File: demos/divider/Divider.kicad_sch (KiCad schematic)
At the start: 3 parts

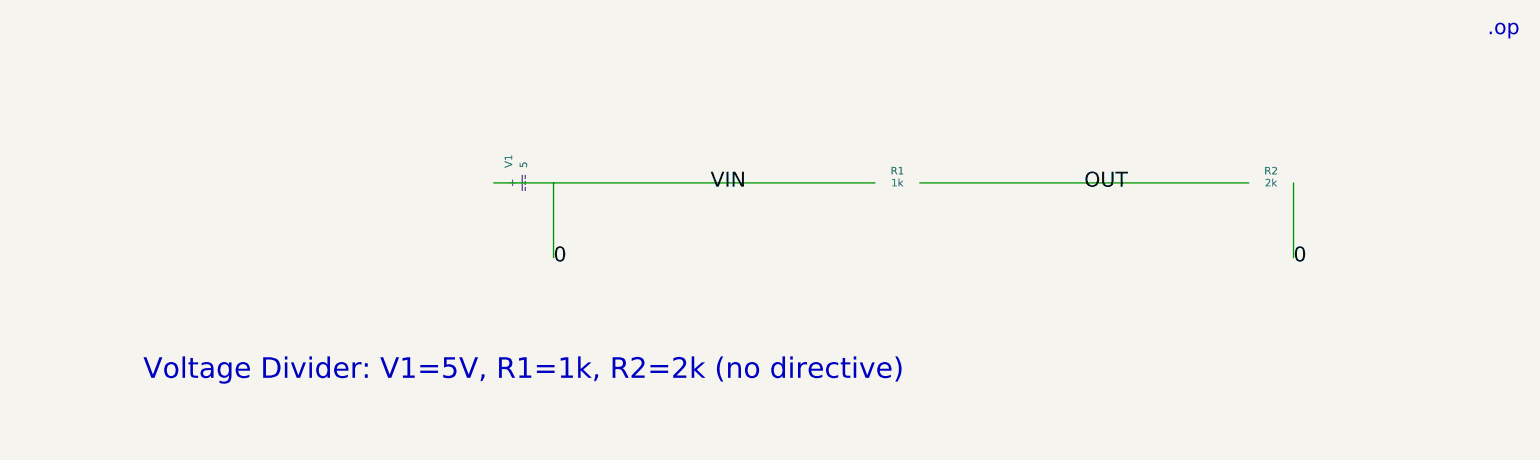
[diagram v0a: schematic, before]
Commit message: feat: Add custom symbol generation for KiCad
- Introduced a new symbol writer module to generate KiCad symbols from specifications.
- Added support for creating custom symbols in a private library, including NE555 and L78L05 components.
- Implemented a command to create symbols from specifications and integrate them into the project's symbol library.
- Developed tests for creating symbols and drawing circuits with custom components, ensuring proper functionality and compliance with ERC.
- Created example scripts for generating symbols from datasheets, specifically for the RP2040 microcontroller.
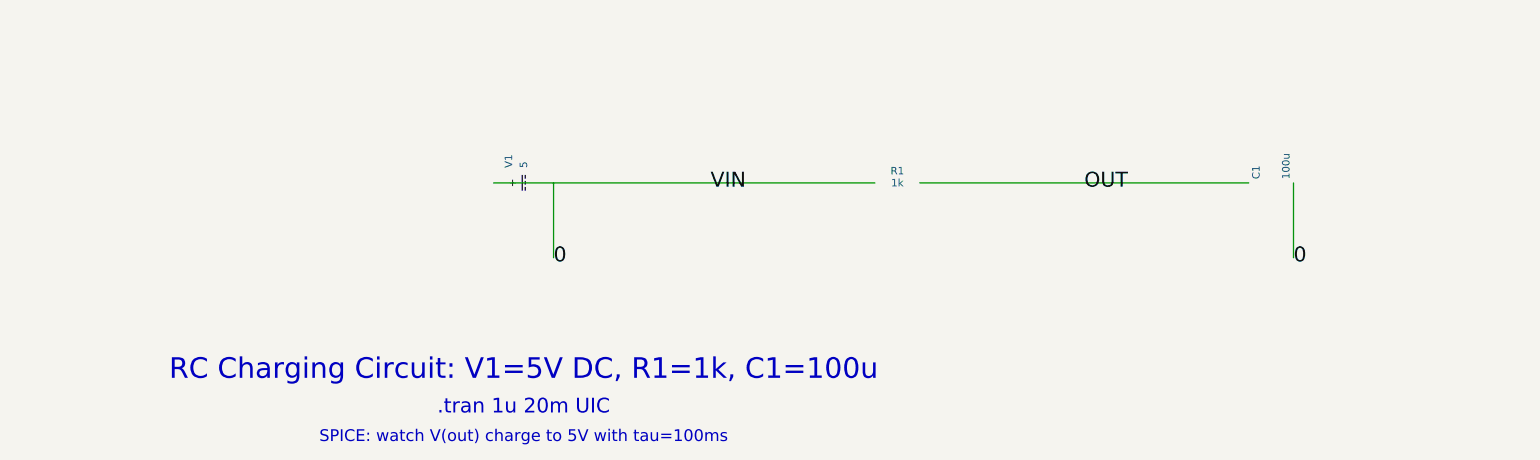
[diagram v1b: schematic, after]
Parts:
- removed R2: 2k, symbol Device:R
- added C1: 100u, symbol Device:C
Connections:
- net 0: now also C1.2
- net OUT: now also C1.1
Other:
- note added: ".tran 1u 20m UIC"
- note added: "RC Charging Circuit: V1=5V DC, R1=1k, C1=100u"
- note added: "SPICE: watch V(out) charge to 5V with tau=100ms"
- note removed: ".op"
- note removed: "Voltage Divider: V1=5V, R1=1k, R2=2k (no directive)"
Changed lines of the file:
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@@
 		(title "Voltage Divider")
 	)
-	(text "Voltage Divider: V1=5V, R1=1k, R2=2k (no directive)"
+	(text ".tran 1u 20m UIC"
+		(exclude_from_sim no)
+		(at 63.5 114.3 0)
+		(effects
+			(font
+				(size 2.5 2.5)
+			)
+		)
+	)
+	(text "RC Charging Circuit: V1=5V DC, R1=1k, C1=100u"
 		(exclude_from_sim no)
 		(at 63.5 107.95 0)
@@
 		)
 	)
-	(text ".op"
-		(exclude_from_sim no)
-		(at 230 50 0)
-		(effects
-			(font
-				(size 2.54 2.54)
-			)
+	(text "SPICE: watch V(out) charge to 5V with tau=100ms"
+		(exclude_from_sim no)
+		(at 63.5 119.38 0)
+		(effects
+			(font
+				(size 2 2)
+			)
+		)
+	)
+	(wire
+		(pts
+			(xy 130.81 76.2) (xy 186.69 76.2)
+		)
+		(stroke
+			(width 0)
+			(type default)
+		)
+	)
+	(wire
+		(pts
+			(xy 58.42 76.2) (xy 123.19 76.2)
+		)
+		(stroke
+			(width 0)
+			(type default)
 		)
 	)
@@
 		)
 	)
-	(wire
-		(pts
-			(xy 130.81 76.2) (xy 186.69 76.2)
-		)
-		(stroke
-			(width 0)
-			(type default)
-		)
-	)
-	(wire
-		(pts
-			(xy 58.42 76.2) (xy 123.19 76.2)
-		)
-		(stroke
-			(width 0)
-			(type default)
+	(label "0"
+		(at 68.58 88.9 0)
+		(effects
+			(font
+				(size 2.54 2.54)
+			)
+		)
+	)
+	(label "OUT"
+		(at 158.75 76.2 0)
+		(effects
+			(font
+				(size 2.54 2.54)
+			)
+		)
+	)
+	(label "0"
+		(at 194.31 88.9 0)
+		(effects
+			(font
+				(size 2.54 2.54)
+			)
 		)
 	)
 	(label "VIN"
 		(at 95.25 76.2 0)
-		(effects
-			(font
-				(size 2.54 2.54)
-			)
-		)
-	)
-	(label "0"
-		(at 68.58 88.9 0)
-		(effects
-			(font
-				(size 2.54 2.54)
-			)
-		)
-	)
-	(label "OUT"
-		(at 158.75 76.2 0)
-		(effects
-			(font
-				(size 2.54 2.54)
-			)
-		)
-	)
-	(label "0"
-		(at 194.31 88.9 0)
 		(effects
 			(font
@@
 			)
 		)
+		(pin "2"
+		)
 		(pin "1"
-		)
-		(pin "2"
 		)
 		(instances
@@
 				(path "/91a1d6ab-baa3-4e2f-aded-405b766975b0"
 					(reference "V1")
+					(unit 1)
+				)
+			)
+		)
+	)
+	(symbol
+		(lib_id "Device:C")
+		(at 190.5 76.2 90)
+		(unit 1)
+		(body_style 0)
+		(exclude_from_sim no)
+		(in_bom yes)
+		(on_board yes)
+		(in_pos_files yes)
+		(dnp no)
+		(property "Reference" "C1"
+			(at 187.96 75.565 0)
+			(show_name no)
+			(do_not_autoplace no)
+			(effects
+				(font
+					(size 1.27 1.27)
+				)
+				(justify left)
+			)
+		)
+		(property "Value" "100u"
+			(at 193.04 75.565 0)
+			(show_name no)
+			(do_not_autoplace no)
+			(effects
+				(font
+					(size 1.27 1.27)
+				)
+				(justify left)
+			)
+		)
+		(property "Footprint" ""
+			(at 194.31 75.2348 0)
+			(hide yes)
+			(show_name no)
+			(do_not_autoplace no)
+			(effects
+				(font
+					(size 1.27 1.27)
+				)
+			)
+		)
+		(property "Datasheet" ""
+			(at 190.5 76.2 0)
+			(hide yes)
+			(show_name no)
+			(do_not_autoplace no)
+			(effects
+				(font
+					(size 1.27 1.27)
+				)
+			)
+		)
+		(property "Description" "Unpolarized capacitor"
+			(at 190.5 76.2 0)
+			(hide yes)
+			(show_name no)
+			(do_not_autoplace no)
+			(effects
+				(font
+					(size 1.27 1.27)
+				)
+			)
+		)
+		(pin "2"
+		)
+		(pin "1"
+		)
+		(instances
+			(project "Divider"
+				(path "/91a1d6ab-baa3-4e2f-aded-405b766975b0"
+					(reference "C1")
 					(unit 1)
 				)
@@
 			)
 		)
+		(pin "1"
+		)
 		(pin "2"
-		)
-		(pin "1"
 		)
 		(instances
@@
 					(unit 1)
 				)
-			)
-		)
-	)
-	(symbol
-		(lib_id "Device:R")
-		(at 190.5 76.2 90)
-		(unit 1)
-		(body_style 0)
-		(exclude_from_sim no)
-		(in_bom yes)
-		(on_board yes)
-		(in_pos_files yes)
-		(dnp no)
-		(property "Reference" "R2"
-			(at 190.5 74.168 90)
-			(show_name no)
-			(do_not_autoplace no)
-			(effects
-				(font
-					(size 1.27 1.27)
-				)
-			)
-		)
-		(property "Value" "2k"
-			(at 190.5 76.2 90)
-			(show_name no)
-			(do_not_autoplace no)
-			(effects
-				(font
-					(size 1.27 1.27)
-				)
-			)
-		)
-		(property "Footprint" ""
-			(at 190.5 77.978 90)
-			(hide yes)
-			(show_name no)
-			(do_not_autoplace no)
-			(effects
-				(font
-					(size 1.27 1.27)
-				)
-			)
-		)
-		(property "Datasheet" ""
-			(at 190.5 76.2 0)
-			(hide yes)
-			(show_name no)
-			(do_not_autoplace no)
-			(effects
-				(font
-					(size 1.27 1.27)
-				)
-			)
-		)
-		(property "Description" "Resistor"
-			(at 190.5 76.2 0)
-			(hide yes)
-			(show_name no)
-			(do_not_autoplace no)
-			(effects
-				(font
-					(size 1.27 1.27)
-				)
-			)
-		)
-		(pin "1"
-		)
-		(pin "2"
-		)
-		(instances
-			(project "Divider"
-				(path "/91a1d6ab-baa3-4e2f-aded-405b766975b0"
-					(reference "R2")
-					(unit 1)
-				)
